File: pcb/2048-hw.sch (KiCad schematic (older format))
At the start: 19 parts

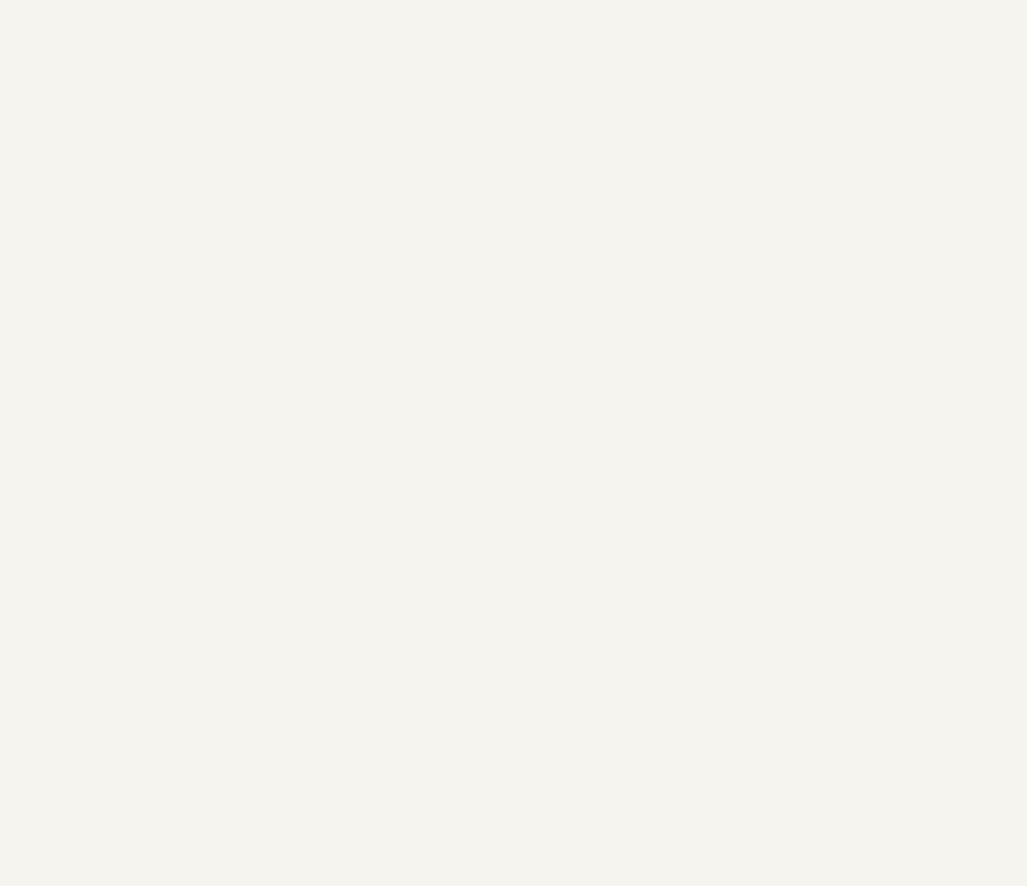
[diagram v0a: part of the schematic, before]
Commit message: Add barebones circuitry for the stm32f303
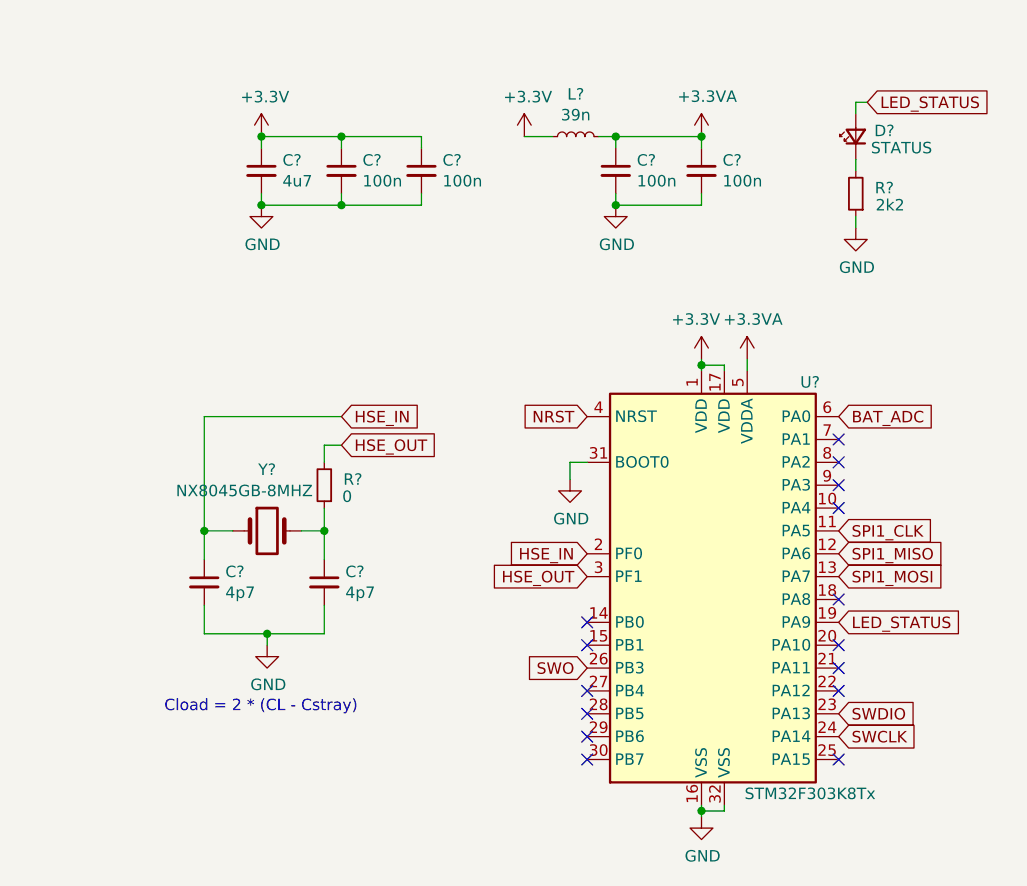
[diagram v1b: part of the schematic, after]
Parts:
- added C?: 4u7, symbol Device:C_Small
- added C? (x4): 100n, symbol Device:C_Small
- added C? (x2): 4p7, symbol Device:C_Small
- added D?: STATUS, symbol Device:LED_Small
- added L?: 39n, symbol Device:L_Small
- added R?: 0, symbol Device:R_Small
- added R?: 2k2, symbol Device:R_Small
- added U?: STM32F303K8Tx, Package_QFP:LQFP-32_7x7mm_P0.8mm, symbol MCU_ST_STM32F3:STM32F303K8Tx
- added Y?: NX8045GB-8MHZ, symbol Device:Crystal
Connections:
- net +3V3: now also C?.1, C?.1, C?.1, L?.1, U?.1 (VDD), U?.17 (VDD)
- net GND: now also C?.2, C?.2, C?.2, C?.2, C?.2, C?.2, C?.2, R?.1, U?.16 (VSS), U?.31 (BOOT0), U?.32 (VSS)
- new net: C?.1, R?.1, Y?.2
- new net: D?.1 (K), R?.2
- new net +3.3VA: C?.1, C?.1, L?.2, U?.5 (VDDA)
- new net BAT_ADC: U?.6 (PA0)
- new net HSE_IN: C?.1, U?.2 (PF0), Y?.1
- new net HSE_OUT: R?.2, U?.3 (PF1)
- new net LED_STATUS: D?.2 (A), U?.19 (PA9)
- new net NRST: U?.4 (NRST)
- new net SPI1_CLK: U?.11 (PA5)
- new net SPI1_MISO: U?.12 (PA6)
- new net SPI1_MOSI: U?.13 (PA7)
- new net SWCLK: U?.24 (PA14)
- new net SWDIO: U?.23 (PA13)
- new net SWO: U?.26 (PB3)
- no-connect marks 2 -> 17
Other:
- note added: "Cload = 2 * (CL - Cstray)"

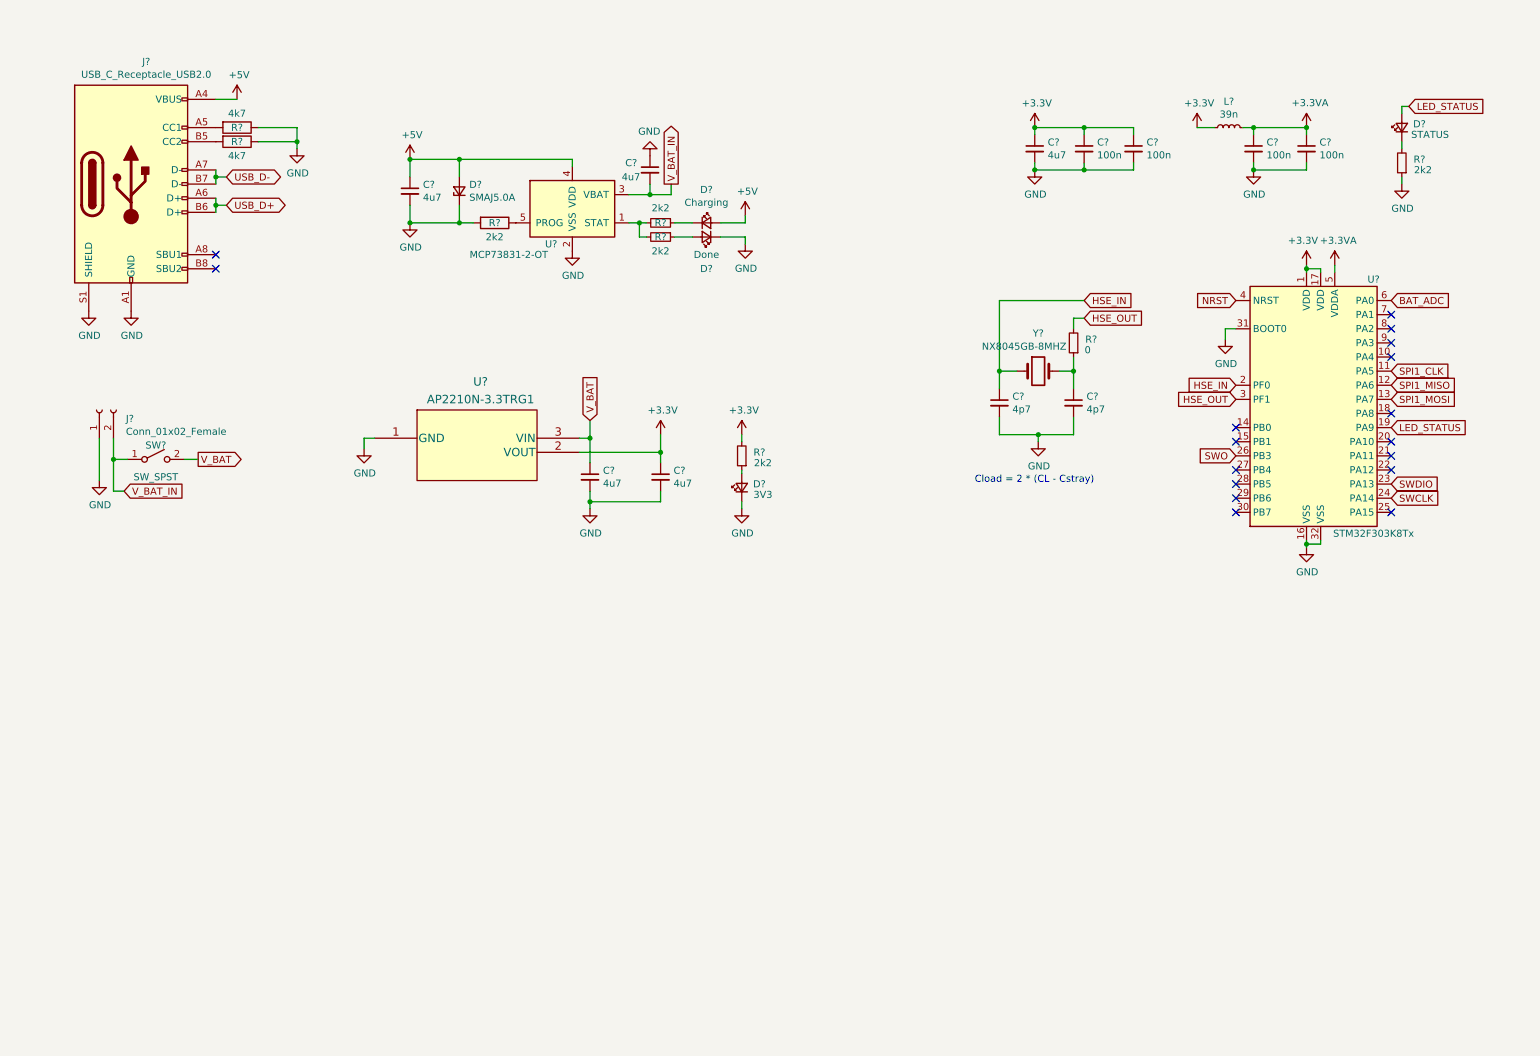
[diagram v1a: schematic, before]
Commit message: Add joystick circuitry
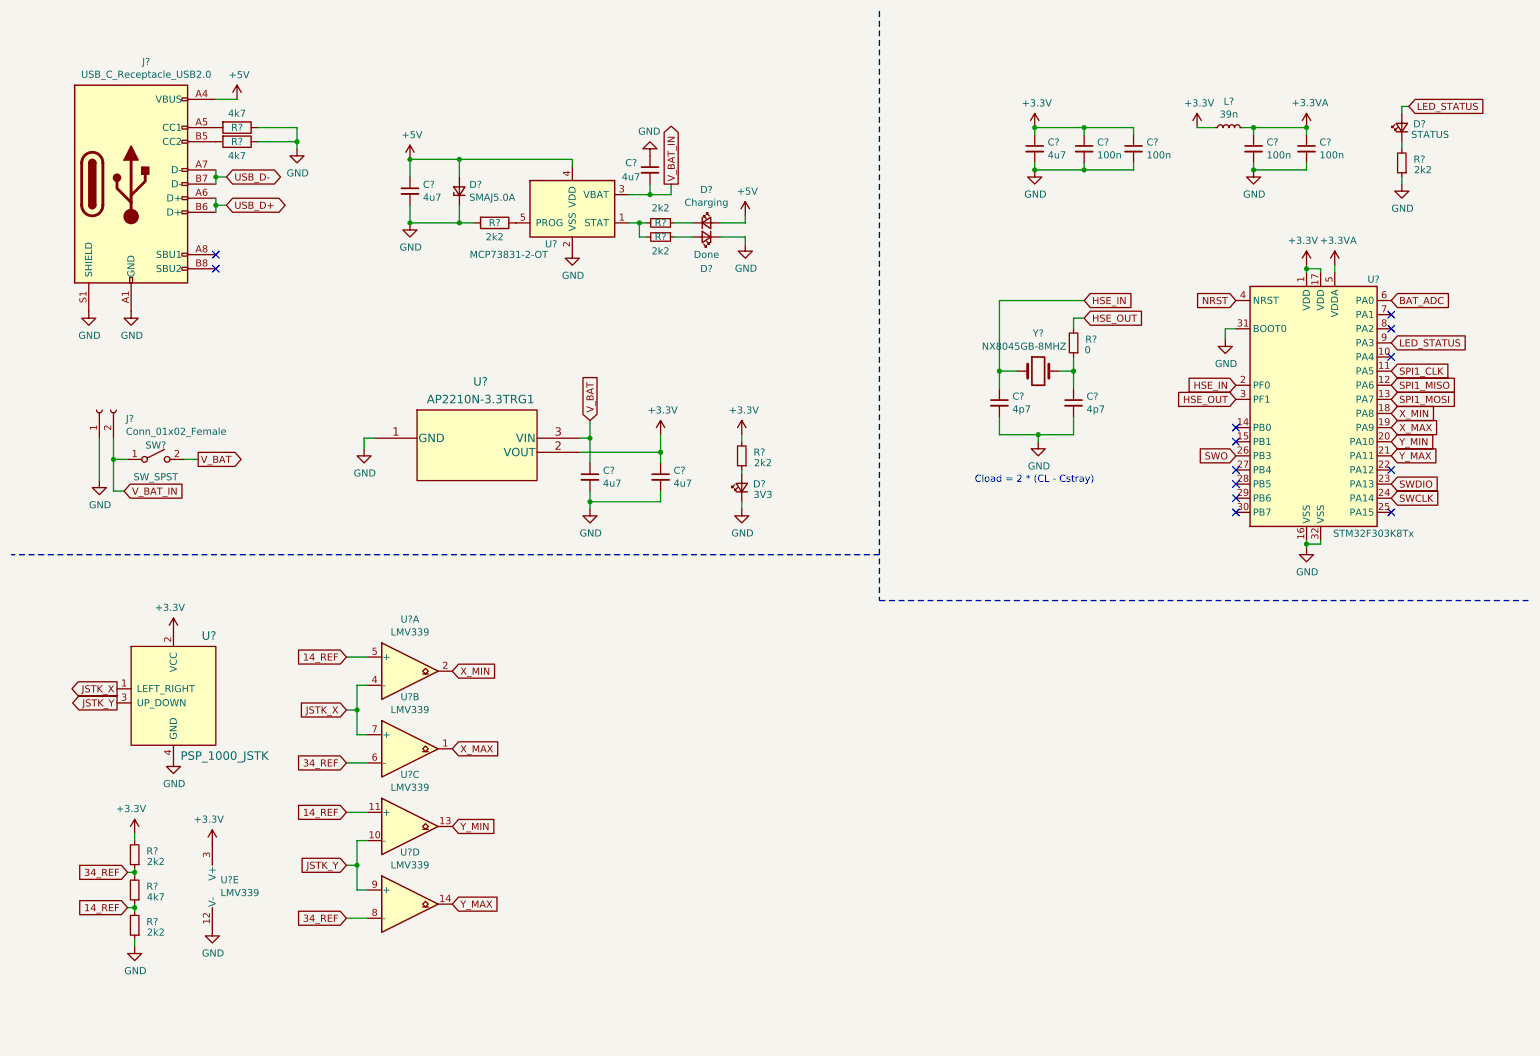
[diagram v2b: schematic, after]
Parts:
- added R? (x2): 2k2, symbol Device:R_Small
- added R?: 4k7, symbol Device:R_Small
- added U?: PSP_1000_JSTK, symbol psp_1000_jstk-hackpackv4:PSP_1000_JSTK-HackPackv4-rescue
- added U? (x5): LMV339, symbol Comparator:LMV339
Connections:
- net +3V3: now also R?.2, U?.2 (VCC), U?.3 (V+)
- net GND: now also R?.1, U?.12 (V-), U?.4 (GND)
- net LED_STATUS: now also U?.9 (PA3); no longer U?.19 (PA9)
- net X_MIN: now reaches U?.18 (PA8)
- net X_MIN: now also U?.2
- net Y_MIN: now reaches U?.20 (PA10)
- net Y_MIN: now also U?.13
- net Y_MAX: now reaches U?.21 (PA11)
- net Y_MAX: now also U?.14
- new net 14_REF: R?.1, R?.2, U?.11 (+), U?.5 (+)
- new net 34_REF: R?.1, R?.2, U?.6 (-), U?.8 (-)
- new net JSTK_X: U?.1 (LEFT_RIGHT), U?.4 (-), U?.7 (+)
- new net JSTK_Y: U?.10 (-), U?.3 (UP_DOWN), U?.9 (+)
- new net X_MAX: U?.1, U?.19 (PA9)
- no-connect marks 17 -> 13
